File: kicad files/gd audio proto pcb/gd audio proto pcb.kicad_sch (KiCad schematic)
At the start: 29 parts, among them J1 Vol I2C, J2 SPKR, J3 Ears, U1 MCP4541T, U2 LM4875

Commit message: 1206 220nF change and added BOM
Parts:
- C1: footprint Resistor_SMD:R_0805_2012Metric -> Resistor_SMD:R_1206_3216Metric
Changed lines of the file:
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@@
       (effects (font (size 1.27 1.27)) (justify left))
     )
-    (property "Footprint" "Resistor_SMD:R_0805_2012Metric" (id 2) (at 157.48 80.01 0)
+    (property "Footprint" "Resistor_SMD:R_1206_3216Metric" (id 2) (at 157.48 80.01 0)
       (effects (font (size 1.27 1.27)) hide)
     )
@@
     )
     (path "/00000000-0000-0000-0000-000061f55caf"
-      (reference "C1") (unit 1) (value "220n") (footprint "Resistor_SMD:R_0805_2012Metric")
+      (reference "C1") (unit 1) (value "220n") (footprint "Resistor_SMD:R_1206_3216Metric")
     )
     (path "/00000000-0000-0000-0000-000061f59587"

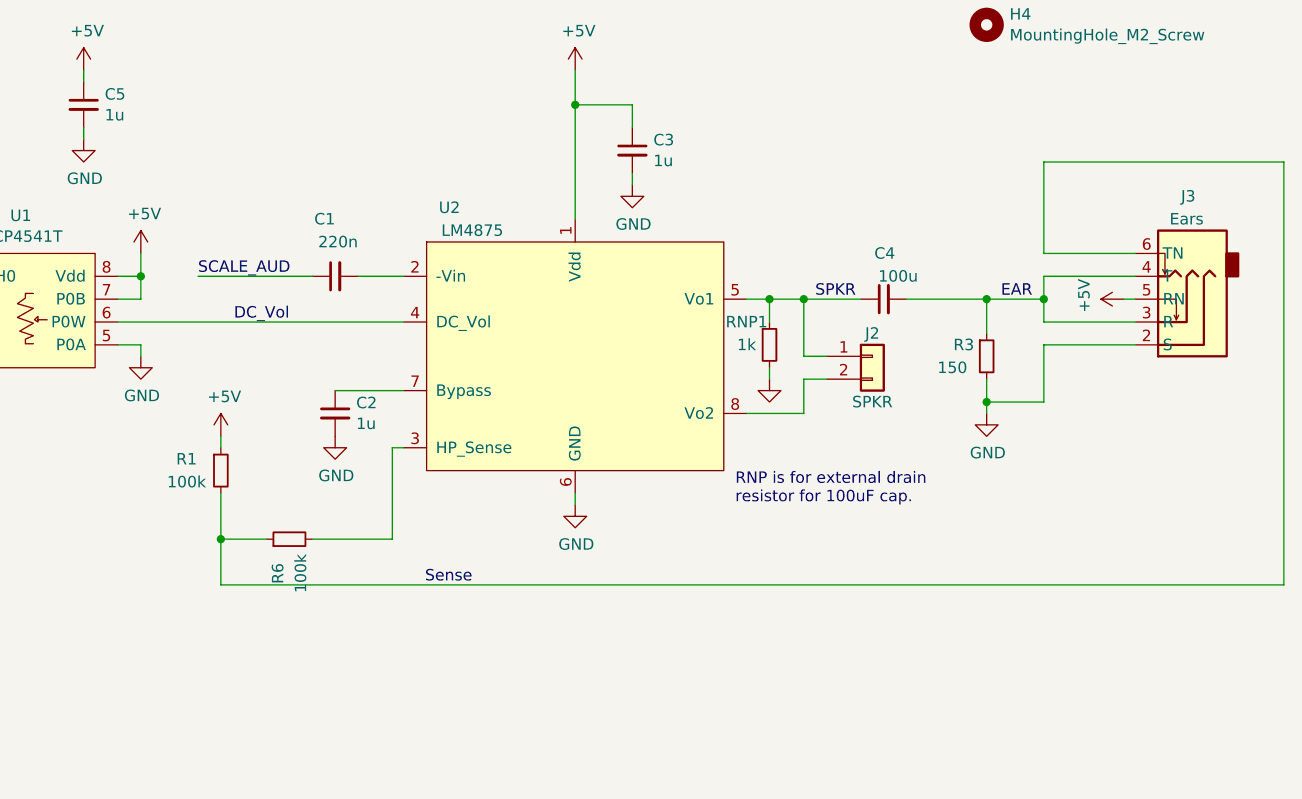
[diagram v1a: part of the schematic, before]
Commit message: fixed Headphone sense before generating gerbers
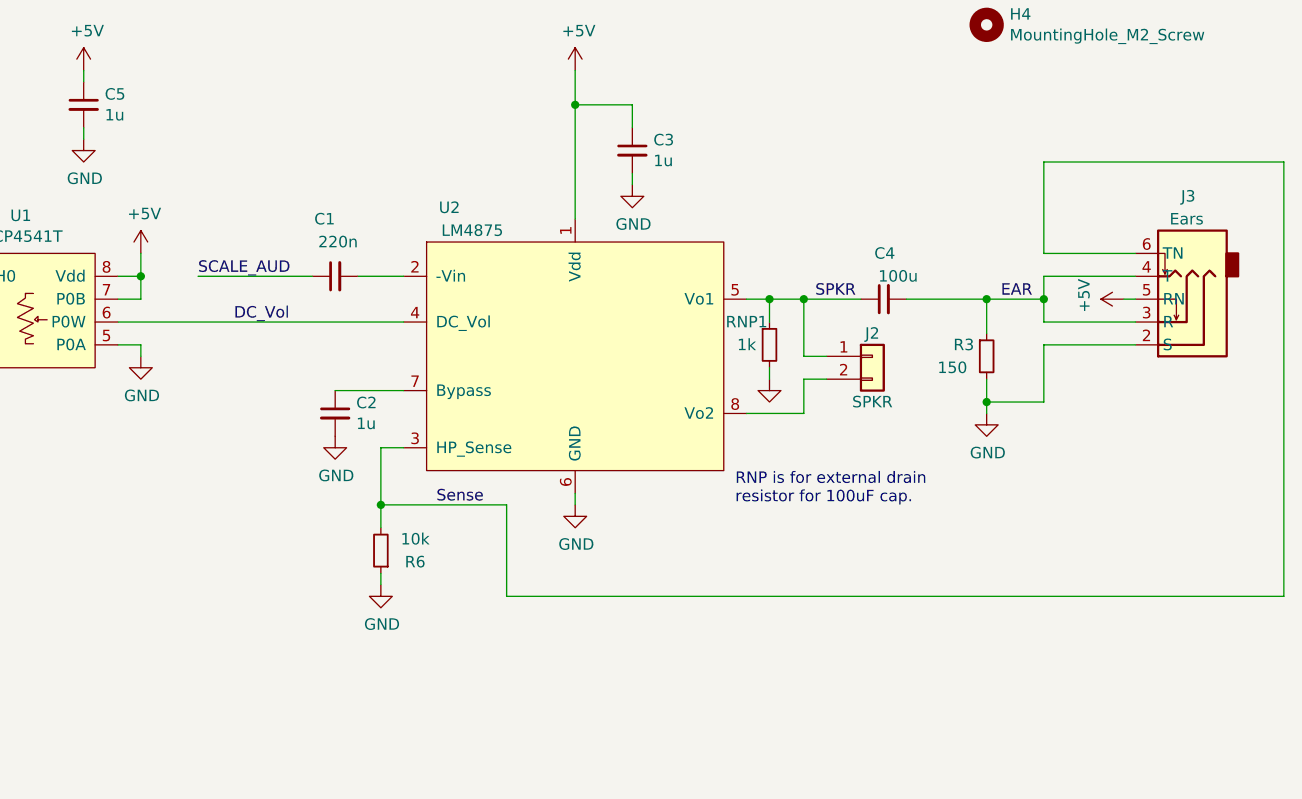
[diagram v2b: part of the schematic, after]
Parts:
- removed R1: 100k, Resistor_SMD:R_0805_2012Metric, symbol My_Library:R_0805
- R6: value 100k -> 10k
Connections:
- net GND: now also R6.1
- net Sense: now also R6.2, U2.3 (HP_Sense); no longer R6.1
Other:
- moved on the sheet: R6
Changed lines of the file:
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@@
   (junction (at 184.15 60.96) (diameter 0) (color 0 0 0 0)
   )
+  (junction (at 162.56 105.41) (diameter 0) (color 0 0 0 0)
+  )
   (junction (at 209.55 82.55) (diameter 0) (color 0 0 0 0)
   )
@@
   (junction (at 135.89 80.01) (diameter 0) (color 0 0 0 0)
   )
-  (junction (at 144.78 109.22) (diameter 0) (color 0 0 0 0)
-  )
-  (wire (pts (xy 144.78 114.3) (xy 262.89 114.3))
-    (stroke (width 0) (type default) (color 0 0 0 0))
-  )
   (wire (pts (xy 63.5 83.82) (xy 74.93 83.82))
     (stroke (width 0) (type default) (color 0 0 0 0))
@@
     (stroke (width 0) (type default) (color 0 0 0 0))
   )
+  (wire (pts (xy 176.53 115.57) (xy 262.89 115.57))
+    (stroke (width 0) (type default) (color 0 0 0 0))
+  )
   (wire (pts (xy 62.23 113.03) (xy 62.23 114.3))
     (stroke (width 0) (type default) (color 0 0 0 0))
@@
     (stroke (width 0) (type default) (color 0 0 0 0))
   )
-  (wire (pts (xy 144.78 114.3) (xy 144.78 109.22))
-    (stroke (width 0) (type default) (color 0 0 0 0))
-  )
-  (wire (pts (xy 144.78 104.14) (xy 144.78 109.22))
-    (stroke (width 0) (type default) (color 0 0 0 0))
-  )
   (wire (pts (xy 40.64 97.79) (xy 53.34 97.79))
     (stroke (width 0) (type default) (color 0 0 0 0))
@@
     (stroke (width 0) (type default) (color 0 0 0 0))
   )
+  (wire (pts (xy 162.56 105.41) (xy 162.56 107.95))
+    (stroke (width 0) (type default) (color 0 0 0 0))
+  )
   (wire (pts (xy 245.11 82.55) (xy 246.38 82.55))
     (stroke (width 0) (type default) (color 0 0 0 0))
@@
     (stroke (width 0) (type default) (color 0 0 0 0))
   )
+  (wire (pts (xy 162.56 99.06) (xy 162.56 105.41))
+    (stroke (width 0) (type default) (color 0 0 0 0))
+  )
   (wire (pts (xy 135.89 80.01) (xy 133.35 80.01))
     (stroke (width 0) (type default) (color 0 0 0 0))
@@
     (stroke (width 0) (type default) (color 0 0 0 0))
   )
-  (wire (pts (xy 163.83 109.22) (xy 154.94 109.22))
-    (stroke (width 0) (type default) (color 0 0 0 0))
-  )
   (wire (pts (xy 74.93 34.29) (xy 74.93 36.83))
     (stroke (width 0) (type default) (color 0 0 0 0))
   )
+  (wire (pts (xy 262.89 67.31) (xy 262.89 115.57))
+    (stroke (width 0) (type default) (color 0 0 0 0))
+  )
   (wire (pts (xy 133.35 36.83) (xy 139.7 36.83))
     (stroke (width 0) (type default) (color 0 0 0 0))
@@
     (stroke (width 0) (type default) (color 0 0 0 0))
   )
-  (wire (pts (xy 262.89 67.31) (xy 262.89 114.3))
-    (stroke (width 0) (type default) (color 0 0 0 0))
-  )
-  (wire (pts (xy 144.78 99.06) (xy 144.78 97.79))
-    (stroke (width 0) (type default) (color 0 0 0 0))
-  )
   (wire (pts (xy 236.22 87.63) (xy 236.22 93.98))
     (stroke (width 0) (type default) (color 0 0 0 0))
@@
     (stroke (width 0) (type default) (color 0 0 0 0))
   )
-  (wire (pts (xy 144.78 109.22) (xy 149.86 109.22))
-    (stroke (width 0) (type default) (color 0 0 0 0))
-  )
   (wire (pts (xy 40.64 96.52) (xy 40.64 97.79))
     (stroke (width 0) (type default) (color 0 0 0 0))
@@
     (stroke (width 0) (type default) (color 0 0 0 0))
   )
+  (wire (pts (xy 162.56 105.41) (xy 176.53 105.41))
+    (stroke (width 0) (type default) (color 0 0 0 0))
+  )
   (wire (pts (xy 40.64 97.79) (xy 40.64 99.06))
     (stroke (width 0) (type default) (color 0 0 0 0))
   )
-  (wire (pts (xy 163.83 99.06) (xy 163.83 109.22))
+  (wire (pts (xy 162.56 113.03) (xy 162.56 114.3))
     (stroke (width 0) (type default) (color 0 0 0 0))
   )
@@
     (stroke (width 0) (type default) (color 0 0 0 0))
   )
-  (wire (pts (xy 165.1 99.06) (xy 163.83 99.06))
-    (stroke (width 0) (type default) (color 0 0 0 0))
-  )
   (wire (pts (xy 209.55 88.9) (xy 212.09 88.9))
     (stroke (width 0) (type default) (color 0 0 0 0))
@@
     (stroke (width 0) (type default) (color 0 0 0 0))
   )
+  (wire (pts (xy 176.53 105.41) (xy 176.53 115.57))
+    (stroke (width 0) (type default) (color 0 0 0 0))
+  )
   (wire (pts (xy 135.89 82.55) (xy 135.89 80.01))
     (stroke (width 0) (type default) (color 0 0 0 0))
@@
   )
   (wire (pts (xy 190.5 60.96) (xy 190.5 63.5))
+    (stroke (width 0) (type default) (color 0 0 0 0))
+  )
+  (wire (pts (xy 162.56 99.06) (xy 165.1 99.06))
     (stroke (width 0) (type default) (color 0 0 0 0))
   )
@@
     (effects (font (size 1.27 1.27)) (justify right bottom))
   )
-  (label "Sense" (at 172.72 114.3 180)
+  (label "Sense" (at 173.99 105.41 180)
     (effects (font (size 1.27 1.27)) (justify right bottom))
   )
@@
     (pin "1")
   )
-  (symbol (lib_id "My_Library:R_0805") (at 144.78 101.6 0) (unit 1)
-    (in_bom yes) (on_board yes)
-    (property "Reference" "R1" (id 0) (at 140.97 100.33 0))
-    (property "Value" "100k" (id 1) (at 140.97 102.87 0))
-    (property "Footprint" "Resistor_SMD:R_0805_2012Metric" (id 2) (at 144.78 101.6 0)
-      (effects (font (size 1.27 1.27)) hide)
-    )
-    (property "Datasheet" "~" (id 3) (at 144.78 101.6 0)
-      (effects (font (size 1.27 1.27)) hide)
-    )
-    (pin "1")
-    (pin "2")
-  )
-  (symbol (lib_id "power:+5V") (at 144.78 97.79 0) (unit 1)
-    (in_bom yes) (on_board yes)
-    (property "Reference" "#PWR0106" (id 0) (at 144.78 101.6 0)
-      (effects (font (size 1.27 1.27)) hide)
-    )
-    (property "Value" "+5V" (id 1) (at 145.161 93.3958 0))
-    (property "Footprint" "" (id 2) (at 144.78 97.79 0)
-      (effects (font (size 1.27 1.27)) hide)
-    )
-    (property "Datasheet" "" (id 3) (at 144.78 97.79 0)
-      (effects (font (size 1.27 1.27)) hide)
-    )
-    (pin "1")
-  )
   (symbol (lib_id "Device:C_Small") (at 218.44 82.55 90) (unit 1)
     (in_bom yes) (on_board yes)
@@
     (pin "1")
   )
+  (symbol (lib_id "power:GND") (at 162.56 114.3 0) (unit 1)
+    (in_bom yes) (on_board yes)
+    (property "Reference" "#PWR?" (id 0) (at 162.56 120.65 0)
+      (effects (font (size 1.27 1.27)) hide)
+    )
+    (property "Value" "GND" (id 1) (at 162.687 118.6942 0))
+    (property "Footprint" "" (id 2) (at 162.56 114.3 0)
+      (effects (font (size 1.27 1.27)) hide)
+    )
+    (property "Datasheet" "" (id 3) (at 162.56 114.3 0)
+      (effects (font (size 1.27 1.27)) hide)
+    )
+    (pin "1")
+  )
   (symbol (lib_id "Connector:TestPoint") (at 133.35 34.29 0) (unit 1)
     (in_bom yes) (on_board yes)
@@
     (pin "1")
   )
-  (symbol (lib_id "My_Library:R_0805") (at 152.4 109.22 90) (unit 1)
-    (in_bom yes) (on_board yes)
-    (property "Reference" "R6" (id 0) (at 151.13 113.03 0))
-    (property "Value" "100k" (id 1) (at 153.67 113.03 0))
-    (property "Footprint" "Resistor_SMD:R_0805_2012Metric" (id 2) (at 152.4 109.22 0)
-      (effects (font (size 1.27 1.27)) hide)
-    )
-    (property "Datasheet" "~" (id 3) (at 152.4 109.22 0)
+  (symbol (lib_id "My_Library:R_0805") (at 162.56 110.49 180) (unit 1)
+    (in_bom yes) (on_board yes)
+    (property "Reference" "R6" (id 0) (at 166.37 111.76 0))
+    (property "Value" "10k" (id 1) (at 166.37 109.22 0))
+    (property "Footprint" "Resistor_SMD:R_0805_2012Metric" (id 2) (at 162.56 110.49 0)
+      (effects (font (size 1.27 1.27)) hide)
+    )
+    (property "Datasheet" "~" (id 3) (at 162.56 110.49 0)
       (effects (font (size 1.27 1.27)) hide)
     )
@@
       (reference "#PWR0105") (unit 1) (value "GND") (footprint "")
     )
-    (path "/00000000-0000-0000-0000-000061f5f98f"
-      (reference "#PWR0106") (unit 1) (value "+5V") (footprint "")
-    )
     (path "/00000000-0000-0000-0000-000061f6a26d"
       (reference "#PWR0107") (unit 1) (value "GND") (footprint "")
@@
       (reference "#PWR0118") (unit 1) (value "+5V") (footprint "")
     )
+    (path "/0ebe1bf8-94e1-4a99-b976-3001b99dc87f"
+      (reference "#PWR?") (unit 1) (value "GND") (footprint "")
+    )
     (path "/00000000-0000-0000-0000-000061f55caf"
       (reference "C1") (unit 1) (value "220n") (footprint "Resistor_SMD:R_1206_3216Metric")
@@
       (reference "J3") (unit 1) (value "Ears") (footprint "Connector_Audio:Jack_3.5mm_PJ311_Horizontal")
     )
-    (path "/00000000-0000-0000-0000-000061f5d665"
-      (reference "R1") (unit 1) (value "100k") (footprint "Resistor_SMD:R_0805_2012Metric")
-    )
     (path "/8adbb741-2dfd-4350-8554-f342663361ff"
       (reference "R2") (unit 1) (value "1k") (footprint "Resistor_SMD:R_0805_2012Metric")
@@
     )
     (path "/5cd66c28-1bec-42a9-a08d-5c3ea4abece4"
-      (reference "R6") (unit 1) (value "100k") (footprint "Resistor_SMD:R_0805_2012Metric")
+      (reference "R6") (unit 1) (value "10k") (footprint "Resistor_SMD:R_0805_2012Metric")
     )
     (path "/00000000-0000-0000-0000-000061fe05ac"

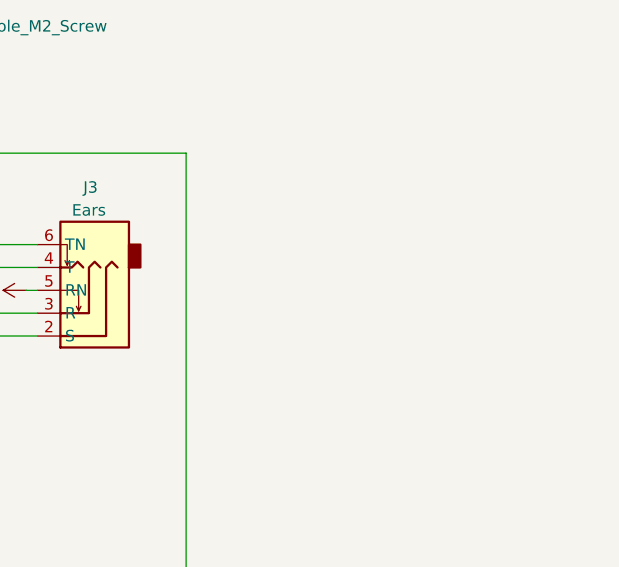
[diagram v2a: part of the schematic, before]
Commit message: ibom for audio and adding some hierarchical labels (wrong branch)
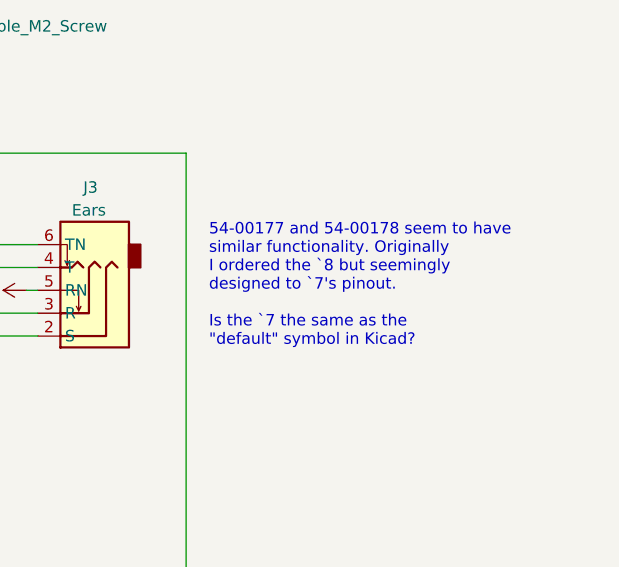
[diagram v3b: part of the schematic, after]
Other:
- note added: "54-00177 and 54-00178 seem to have similar functionality. Originally I ordered the `8 but seemingly designed to `7's pinout. Is the `7 the same as the "default" symbol in Kicad?"
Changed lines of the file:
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@@
+    (effects (font (size 1.27 1.27)) (justify left bottom))
+  )
+  (text "54-00177 and 54-00178 seem to have\nsimilar functionality. Originally \nI ordered the `8 but seemingly \ndesigned to `7's pinout.\n\nIs the `7 the same as the \n\"default\" symbol in Kicad?"
+    (at 265.43 88.9 0)
     (effects (font (size 1.27 1.27)) (justify left bottom))
   )
@@
       (effects (font (size 1.27 1.27)) hide)
     )
-    (property "Datasheet" "https://tensility.s3.amazonaws.com/uploads/pdffiles/54-00177.pdf?X-Amz-Expires=600&X-Amz-Date=20220124T060305Z&X-Amz-Algorithm=AWS4-HMAC-SHA256&X-Amz-Credential=AKIAIS2S4WRDQDSWDRZQ%2F20220124%2Fus-west-2%2Fs3%2Faws4_request&X-Amz-SignedHeaders=host&X-Amz-Signature=f29aa2fcc9e95073a664c3cd2871b5bf87d9725ad5d792b012eee0a99475bfa2" (id 3) (at 251.46 85.09 0)
+    (property "Datasheet" "https://tensility.s3.amazonaws.com/uploads/pdffiles/54-00178.pdf" (id 3) (at 251.46 85.09 0)
       (effects (font (size 1.27 1.27)) hide)
     )
